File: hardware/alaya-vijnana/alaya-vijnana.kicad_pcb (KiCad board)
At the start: 2 copper layers, 2 parts, among them U2 nRF52840, X1 IQD_85SMX

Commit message: schematics done outside of cluster to main connectors, PCB laid out
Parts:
- added C1: 12pF, Capacitor_SMD:C_0603_1608Metric_Pad1.08x0.95mm_HandSolder, F.Cu at (532.9, 137.2)
- added C10: 100pF, Capacitor_SMD:C_0603_1608Metric_Pad1.08x0.95mm_HandSolder, F.Cu at (537.3, 137.2)
- added C11: 100pF, Capacitor_SMD:C_0603_1608Metric_Pad1.08x0.95mm_HandSolder, F.Cu at (537.3, 139.7)
- added C12: 820pF, Capacitor_SMD:C_0603_1608Metric_Pad1.08x0.95mm_HandSolder, F.Cu at (537.3, 142.2)
- added C13: 4.7uF, Capacitor_SMD:C_0603_1608Metric_Pad1.08x0.95mm_HandSolder, F.Cu at (537.3, 144.7)
- added C14: 1uF, Capacitor_SMD:C_0603_1608Metric_Pad1.08x0.95mm_HandSolder, F.Cu at (537.3, 147.3)
- added C15: 47nF, Capacitor_SMD:C_0603_1608Metric_Pad1.08x0.95mm_HandSolder, F.Cu at (537.3, 149.8)
- added C16: 4.7uF, Capacitor_SMD:C_0603_1608Metric_Pad1.08x0.95mm_HandSolder, F.Cu at (537.3, 152.3)
- added C17: 4.7uF, Capacitor_SMD:C_0603_1608Metric_Pad1.08x0.95mm_HandSolder, F.Cu at (537.3, 154.8)
- added C18: 1uf, Capacitor_SMD:C_0603_1608Metric_Pad1.08x0.95mm_HandSolder, F.Cu at (537.3, 157.3)
- added C19: 100nF, Capacitor_SMD:C_0603_1608Metric_Pad1.08x0.95mm_HandSolder, F.Cu at (541.6, 137.2)
- added C2: 12pF, Capacitor_SMD:C_0603_1608Metric_Pad1.08x0.95mm_HandSolder, F.Cu at (532.9, 139.7)
- added C20: 100nF, Capacitor_SMD:C_0603_1608Metric_Pad1.08x0.95mm_HandSolder, F.Cu at (541.6, 139.7)
- added C21: 100nF, Capacitor_SMD:C_0603_1608Metric_Pad1.08x0.95mm_HandSolder, F.Cu at (541.6, 142.2)
- added C22: 4.7uF, Capacitor_SMD:C_0603_1608Metric_Pad1.08x0.95mm_HandSolder, F.Cu at (541.6, 144.7)
- added C23: 12pF, Capacitor_SMD:C_0603_1608Metric_Pad1.08x0.95mm_HandSolder, F.Cu at (541.6, 147.3)
- added C24: 12pF, Capacitor_SMD:C_0603_1608Metric_Pad1.08x0.95mm_HandSolder, F.Cu at (541.6, 149.8)
- added C25: 4.7uF, Capacitor_SMD:C_0603_1608Metric_Pad1.08x0.95mm_HandSolder, F.Cu at (541.6, 152.3)
- added C26: 1uf, Capacitor_SMD:C_0603_1608Metric_Pad1.08x0.95mm_HandSolder, F.Cu at (532.9, 64.8)
- added C27: 100nF, Capacitor_SMD:C_0603_1608Metric_Pad1.08x0.95mm_HandSolder, F.Cu at (532.9, 67.3)
- added C28: 100nF, Capacitor_SMD:C_0603_1608Metric_Pad1.08x0.95mm_HandSolder, F.Cu at (532.9, 69.8)
- added C29: 100nF, Capacitor_SMD:C_0603_1608Metric_Pad1.08x0.95mm_HandSolder, F.Cu at (532.9, 72.3)
- added C3: 1uF, Capacitor_SMD:C_0603_1608Metric_Pad1.08x0.95mm_HandSolder, F.Cu at (532.9, 142.2)
- added C30: 4.7uF, Capacitor_SMD:C_0603_1608Metric_Pad1.08x0.95mm_HandSolder, F.Cu at (532.9, 74.9)
- added C31: 12pF, Capacitor_SMD:C_0603_1608Metric_Pad1.08x0.95mm_HandSolder, F.Cu at (532.9, 77.4)
- added C32: 12pF, Capacitor_SMD:C_0603_1608Metric_Pad1.08x0.95mm_HandSolder, F.Cu at (532.9, 79.9)
- added C33: 100pF, Capacitor_SMD:C_0603_1608Metric_Pad1.08x0.95mm_HandSolder, F.Cu at (532.9, 82.4)
- added C34: 100pF, Capacitor_SMD:C_0603_1608Metric_Pad1.08x0.95mm_HandSolder, F.Cu at (532.9, 84.9)
- added C35: 820pF, Capacitor_SMD:C_0603_1608Metric_Pad1.08x0.95mm_HandSolder, F.Cu at (537.3, 64.8)
- added C36: 4.7uF, Capacitor_SMD:C_0603_1608Metric_Pad1.08x0.95mm_HandSolder, F.Cu at (537.3, 67.3)
- added C37: 4.7uF, Capacitor_SMD:C_0603_1608Metric_Pad1.08x0.95mm_HandSolder, F.Cu at (537.3, 69.8)
- added C38: 4.7uF, Capacitor_SMD:C_0603_1608Metric_Pad1.08x0.95mm_HandSolder, F.Cu at (537.3, 72.3)
- added C39: 1uF, Capacitor_SMD:C_0603_1608Metric_Pad1.08x0.95mm_HandSolder, F.Cu at (537.3, 74.9)
- added C4: 4.7uF, Capacitor_SMD:C_0603_1608Metric_Pad1.08x0.95mm_HandSolder, F.Cu at (532.9, 144.7)
- added C40: 47nF, Capacitor_SMD:C_0603_1608Metric_Pad1.08x0.95mm_HandSolder, F.Cu at (537.3, 77.4)
- added C41: 12pF, Capacitor_SMD:C_0603_1608Metric_Pad1.08x0.95mm_HandSolder, F.Cu at (537.3, 79.9)
- added C42: 12pF, Capacitor_SMD:C_0603_1608Metric_Pad1.08x0.95mm_HandSolder, F.Cu at (537.3, 82.4)
- added C43: 10uF, Capacitor_SMD:C_0603_1608Metric_Pad1.08x0.95mm_HandSolder, F.Cu at (537.3, 84.9)
- added C44: 1uF, Capacitor_SMD:C_0603_1608Metric_Pad1.08x0.95mm_HandSolder, F.Cu at (541.6, 64.8)
- added C45: 4.7uF, Capacitor_SMD:C_0603_1608Metric_Pad1.08x0.95mm_HandSolder, F.Cu at (541.6, 67.3)
- added C46: 4.7uF, Capacitor_SMD:C_0603_1608Metric_Pad1.08x0.95mm_HandSolder, F.Cu at (541.6, 69.8)
- added C47: 4.7uF, Capacitor_SMD:C_0603_1608Metric_Pad1.08x0.95mm_HandSolder, F.Cu at (541.6, 72.3)
- added C48: 0.8pF, Capacitor_SMD:C_0603_1608Metric_Pad1.08x0.95mm_HandSolder, F.Cu at (541.6, 74.9)
- added C49: 0.5pF, Capacitor_SMD:C_0603_1608Metric_Pad1.08x0.95mm_HandSolder, F.Cu at (541.6, 77.4)
- added C5: 4.7uF, Capacitor_SMD:C_0603_1608Metric_Pad1.08x0.95mm_HandSolder, F.Cu at (532.9, 147.3)
- added C50: N.C., Capacitor_SMD:C_0603_1608Metric_Pad1.08x0.95mm_HandSolder, F.Cu at (541.6, 79.9)
- added C6: 0.8pF, Capacitor_SMD:C_0603_1608Metric_Pad1.08x0.95mm_HandSolder, F.Cu at (532.9, 149.8)
- added C7: 0.5pF, Capacitor_SMD:C_0603_1608Metric_Pad1.08x0.95mm_HandSolder, F.Cu at (532.9, 152.3)
- added C8: N.C., Capacitor_SMD:C_0603_1608Metric_Pad1.08x0.95mm_HandSolder, F.Cu at (532.9, 154.8)
- added C9: 10uF, Capacitor_SMD:C_0603_1608Metric_Pad1.08x0.95mm_HandSolder, F.Cu at (532.9, 157.3)
- added D1: D, Diode_SMD:D_0603_1608Metric_Pad1.05x0.95mm_HandSolder, B.Cu at (236.0, 16.9)
- added D10: D, Diode_SMD:D_0603_1608Metric_Pad1.05x0.95mm_HandSolder, B.Cu at (199.5, 14.0)
- added D11: D, Diode_SMD:D_0603_1608Metric_Pad1.05x0.95mm_HandSolder, B.Cu at (242.8, 22.6)
- added D12: D, Diode_SMD:D_0603_1608Metric_Pad1.05x0.95mm_HandSolder, B.Cu at (183.8, 23.6)
- added D13: D, Diode_SMD:D_0603_1608Metric_Pad1.05x0.95mm_HandSolder, B.Cu at (248.2, 16.4)
- added D14: D, Diode_SMD:D_0603_1608Metric_Pad1.05x0.95mm_HandSolder, B.Cu at (157.5, 6.88)
- added D15: D, Diode_SMD:D_0603_1608Metric_Pad1.05x0.95mm_HandSolder, B.Cu at (247.8, 23.6)
- added D16: D, Diode_SMD:D_0603_1608Metric_Pad1.05x0.95mm_HandSolder, B.Cu at (176.2, 15.1)
- added D17: D, Diode_SMD:D_0603_1608Metric_Pad1.05x0.95mm_HandSolder, B.Cu at (158.0, 20.9)
- added D18: D, Diode_SMD:D_0603_1608Metric_Pad1.05x0.95mm_HandSolder, B.Cu at (256.2, 22.9)
- added D19: D, Diode_SMD:D_0603_1608Metric_Pad1.05x0.95mm_HandSolder, B.Cu at (243.0, 32.9)
- added D2: D, Diode_SMD:D_0603_1608Metric_Pad1.05x0.95mm_HandSolder, B.Cu at (156.0, 13.6)
- added D20: D, Diode_SMD:D_0603_1608Metric_Pad1.05x0.95mm_HandSolder, B.Cu at (168.2, 20.4)
- added D21: D, Diode_SMD:D_0603_1608Metric_Pad1.05x0.95mm_HandSolder, B.Cu at (259.8, 31.4)
- added D22: D, Diode_SMD:D_0603_1608Metric_Pad1.05x0.95mm_HandSolder, B.Cu at (257.0, 15.4)
- added D23: D, Diode_SMD:D_0603_1608Metric_Pad1.05x0.95mm_HandSolder, B.Cu at (158.8, 27.1)
- added D24: D, Diode_SMD:D_0603_1608Metric_Pad1.05x0.95mm_HandSolder, B.Cu at (252.2, 28.6)
- added D25: D, Diode_SMD:D_0603_1608Metric_Pad1.05x0.95mm_HandSolder, B.Cu at (193.2, 12.4)
- added D26: D, Diode_SMD:D_0603_1608Metric_Pad1.05x0.95mm_HandSolder, B.Cu at (164.5, 25.6)
- added D27: D, Diode_SMD:D_0603_1608Metric_Pad1.05x0.95mm_HandSolder, B.Cu at (235.5, 24.1)
- added D28: D, Diode_SMD:D_0603_1608Metric_Pad1.05x0.95mm_HandSolder, B.Cu at (262.2, 24.1)
- added D29: D, Diode_SMD:D_0603_1608Metric_Pad1.05x0.95mm_HandSolder, B.Cu at (164.1, 36.5)
- added D3: D, Diode_SMD:D_0603_1608Metric_Pad1.05x0.95mm_HandSolder, B.Cu at (240.5, 11.9)
- added D30: D, Diode_SMD:D_0603_1608Metric_Pad1.05x0.95mm_HandSolder, B.Cu at (186.7, 42.6)
- added D31: D, Diode_SMD:D_0603_1608Metric_Pad1.05x0.95mm_HandSolder, B.Cu at (174.9, 30.0)
- added D32: D, Diode_SMD:D_0603_1608Metric_Pad1.05x0.95mm_HandSolder, B.Cu at (178.7, 31.7)
- added D33: D, Diode_SMD:D_0603_1608Metric_Pad1.05x0.95mm_HandSolder, B.Cu at (191.2, 42.7)
- added D34: D, Diode_SMD:D_0603_1608Metric_Pad1.05x0.95mm_HandSolder, B.Cu at (195.2, 44.4)
- added D35: D, Diode_SMD:D_0603_1608Metric_Pad1.05x0.95mm_HandSolder, B.Cu at (206.7, 37.7)
- added D36: D, Diode_SMD:D_0603_1608Metric_Pad1.05x0.95mm_HandSolder, B.Cu at (212.4, 38.7)
- added D37: D, Diode_SMD:D_0603_1608Metric_Pad1.05x0.95mm_HandSolder, B.Cu at (230.2, 42.4)
- added D38: D, Diode_SMD:D_0603_1608Metric_Pad1.05x0.95mm_HandSolder, B.Cu at (223.1, 40.3)
- added D39: D, Diode_SMD:D_0603_1608Metric_Pad1.05x0.95mm_HandSolder, B.Cu at (218.2, 39.2)
- added D4: D, Diode_SMD:D_0603_1608Metric_Pad1.05x0.95mm_HandSolder, B.Cu at (163.5, 6.88)
- added D40: D, Diode_SMD:D_0603_1608Metric_Pad1.05x0.95mm_HandSolder, B.Cu at (230.1, 32.5)
- added D41: D, Diode_SMD:D_0603_1608Metric_Pad1.05x0.95mm_HandSolder, B.Cu at (185.5, 13.4)
- added D42: D, Diode_SMD:D_0603_1608Metric_Pad1.05x0.95mm_HandSolder, B.Cu at (169.5, 13.9)
- added D5: D, Diode_SMD:D_0603_1608Metric_Pad1.05x0.95mm_HandSolder, B.Cu at (232.5, 9.62)
- added D6: D, Diode_SMD:D_0603_1608Metric_Pad1.05x0.95mm_HandSolder, B.Cu at (162.0, 13.4)
- added D7: D, Diode_SMD:D_0603_1608Metric_Pad1.05x0.95mm_HandSolder, B.Cu at (163.8, 20.1)
- added D8: D, Diode_SMD:D_0603_1608Metric_Pad1.05x0.95mm_HandSolder, B.Cu at (226.0, 14.0)
- added D9: D, Diode_SMD:D_0603_1608Metric_Pad1.05x0.95mm_HandSolder, B.Cu at (248.8, 8.88)
- added J1: Bat, Connector_JST:JST_PH_S2B-PH-K_1x02_P2.00mm_Horizontal, F.Cu at (562.7, 156.2)
- added J2: USB_C_Receptacle_USB2.0_16P, Connector_USB:USB_C_Receptacle_GCT_USB4085, F.Cu at (551.0, 155.4)
- added J3: Bat, Connector_JST:JST_PH_S2B-PH-K_1x02_P2.00mm_Horizontal, F.Cu at (562.7, 83.8)
- added J4: USB_C_Receptacle_USB2.0_16P, Connector_USB:USB_C_Receptacle_GCT_USB4085, F.Cu at (551.0, 83.0)
- added L1: 4.7nH, Inductor_SMD:L_0402_1005Metric_Pad0.77x0.64mm_HandSolder, F.Cu at (565.4, 144.5)
- added L2: 10uH, Inductor_SMD:L_0603_1608Metric, F.Cu at (565.8, 137.2)
- added L3: 15nH, Inductor_SMD:L_0603_1608Metric, F.Cu at (565.8, 139.7)
- added L4: 10uH, Inductor_SMD:L_0603_1608Metric, F.Cu at (565.8, 142.2)
- added L5: 15nH, Inductor_SMD:L_0603_1608Metric, F.Cu at (565.8, 64.8)
- added L6: 10uH, Inductor_SMD:L_0603_1608Metric, F.Cu at (565.8, 67.3)
- added L7: 10uH, Inductor_SMD:L_0603_1608Metric, F.Cu at (565.8, 69.8)
- added L8: 4.7nH, Inductor_SMD:L_0402_1005Metric_Pad0.77x0.64mm_HandSolder, F.Cu at (565.4, 72.1)
- added LED1: Charge_LED, PCM_LED_SMD_AKL:LED_1206_3216Metric, F.Cu at (543.7, 160.7)
- added LED2: Charge_LED, PCM_LED_SMD_AKL:LED_1206_3216Metric, F.Cu at (543.7, 88.3)
- added R1: 2k, Resistor_SMD:R_0603_1608Metric_Pad0.98x0.95mm_HandSolder, F.Cu at (541.6, 154.8)
- added R10: 10M, Resistor_SMD:R_0603_1608Metric_Pad0.98x0.95mm_HandSolder, F.Cu at (546.0, 64.8)
- added R11: 10k, Resistor_SMD:R_0603_1608Metric_Pad0.98x0.95mm_HandSolder, F.Cu at (546.0, 67.3)
- added R12: 10k, Resistor_SMD:R_0603_1608Metric_Pad0.98x0.95mm_HandSolder, F.Cu at (546.0, 69.8)
- added R13: 5.1k, Resistor_SMD:R_0603_1608Metric_Pad0.98x0.95mm_HandSolder, F.Cu at (546.0, 72.3)
- added R14: 5.1k, Resistor_SMD:R_0603_1608Metric_Pad0.98x0.95mm_HandSolder, F.Cu at (546.0, 74.9)
- added R2: 10k, Resistor_SMD:R_0603_1608Metric_Pad0.98x0.95mm_HandSolder, F.Cu at (541.6, 157.3)
- added R3: 10k, Resistor_SMD:R_0603_1608Metric_Pad0.98x0.95mm_HandSolder, F.Cu at (546.0, 137.2)
- added R4: 10k, Resistor_SMD:R_0603_1608Metric_Pad0.98x0.95mm_HandSolder, F.Cu at (546.0, 139.7)
- added R5: 10M, Resistor_SMD:R_0603_1608Metric_Pad0.98x0.95mm_HandSolder, F.Cu at (546.0, 142.2)
- added R6: 5.1k, Resistor_SMD:R_0603_1608Metric_Pad0.98x0.95mm_HandSolder, F.Cu at (546.0, 144.7)
- added R7: 5.1k, Resistor_SMD:R_0603_1608Metric_Pad0.98x0.95mm_HandSolder, F.Cu at (546.0, 147.3)
- added R8: 2k, Resistor_SMD:R_0603_1608Metric_Pad0.98x0.95mm_HandSolder, F.Cu at (541.6, 82.4)
- added R9: 10k, Resistor_SMD:R_0603_1608Metric_Pad0.98x0.95mm_HandSolder, F.Cu at (541.6, 84.9)
- added SW1: Power_Switch, Button_Switch_THT:SW_E-Switch_EG1224_SPDT_Angled, B.Cu at (516.4, 156.7)
- added SW10: MX HotSwap, MX_Hotswap:MX-Hotswap-1U, B.Cu at (74.8, 90.9)
- added SW11: MX HotSwap, MX_Hotswap:MX-Hotswap-1U, B.Cu at (93.9, 62.3)
- added SW12: MX HotSwap, MX_Hotswap:MX-Hotswap-1U, B.Cu at (93.9, 81.4)
- added SW13: MX HotSwap, MX_Hotswap:MX-Hotswap-1U, B.Cu at (93.9, 100.4)
- added SW14: MX HotSwap, MX_Hotswap:MX-Hotswap-1U, B.Cu at (112.9, 67.1)
- added SW15: MX HotSwap, MX_Hotswap:MX-Hotswap-1U, B.Cu at (112.9, 86.1)
- added SW16: MX HotSwap, MX_Hotswap:MX-Hotswap-1U, B.Cu at (112.9, 105.2)
- added SW17: MX HotSwap, MX_Hotswap:MX-Hotswap-1U, B.Cu at (151.9, 120.7)
- added SW18: MX HotSwap, MX_Hotswap:MX-Hotswap-2U, B.Cu at (137.6, 145.5)
- added SW19: MX HotSwap, MX_Hotswap:MX-Hotswap-2U, B.Cu at (121.2, 136.0)
- added SW2: MX HotSwap, MX_Hotswap:MX-Hotswap-1U, B.Cu at (36.7, 67.1)
- added SW20: MX HotSwap, MX_Hotswap:MX-Hotswap-1U, B.Cu at (168.4, 130.3)
- added SW21: MX HotSwap, MX_Hotswap:MX-Hotswap-1U, B.Cu at (158.9, 146.8)
- added SW22: MX HotSwap, MX_Hotswap:MX-Hotswap-1U, B.Cu at (149.4, 163.3)
- added SW23: Power_Switch, Button_Switch_THT:SW_E-Switch_EG1224_SPDT_Angled, B.Cu at (506.4, 76.2)
- added SW24: MX HotSwap, MX_Hotswap:MX-Hotswap-1U, B.Cu at (371.5, 71.4)
- added SW25: MX HotSwap, MX_Hotswap:MX-Hotswap-1U, B.Cu at (371.5, 90.5)
- added SW26: MX HotSwap, MX_Hotswap:MX-Hotswap-1U, B.Cu at (371.5, 109.5)
- added SW27: MX HotSwap, MX_Hotswap:MX-Hotswap-1U, B.Cu at (352.4, 61.9)
- added SW28: MX HotSwap, MX_Hotswap:MX-Hotswap-1U, B.Cu at (352.4, 81.0)
- added SW29: MX HotSwap, MX_Hotswap:MX-Hotswap-1U, B.Cu at (352.4, 100.0)
- added SW3: MX HotSwap, MX_Hotswap:MX-Hotswap-1U, B.Cu at (36.7, 86.1)
- added SW30: MX HotSwap, MX_Hotswap:MX-Hotswap-1U, B.Cu at (333.4, 57.1)
- added SW31: MX HotSwap, MX_Hotswap:MX-Hotswap-1U, B.Cu at (333.4, 76.2)
- added SW32: MX HotSwap, MX_Hotswap:MX-Hotswap-1U, B.Cu at (333.4, 95.2)
- added SW33: MX HotSwap, MX_Hotswap:MX-Hotswap-1U, B.Cu at (314.3, 66.7)
- added SW34: MX HotSwap, MX_Hotswap:MX-Hotswap-1U, B.Cu at (314.3, 85.7)
- added SW35: MX HotSwap, MX_Hotswap:MX-Hotswap-1U, B.Cu at (314.3, 104.8)
- added SW36: MX HotSwap, MX_Hotswap:MX-Hotswap-1U, B.Cu at (295.3, 71.4)
- added SW37: MX HotSwap, MX_Hotswap:MX-Hotswap-1U, B.Cu at (295.3, 90.5)
- added SW38: MX HotSwap, MX_Hotswap:MX-Hotswap-1U, B.Cu at (295.3, 109.5)
- added SW39: MX HotSwap, MX_Hotswap:MX-Hotswap-1U, B.Cu at (249.3, 151.1)
- added SW4: MX HotSwap, MX_Hotswap:MX-Hotswap-1U, B.Cu at (36.7, 105.2)
- added SW40: MX HotSwap, MX_Hotswap:MX-Hotswap-2U, B.Cu at (270.5, 149.8)
- added SW41: MX HotSwap, MX_Hotswap:MX-Hotswap-2U, B.Cu at (287.0, 140.3)
- added SW42: MX HotSwap, MX_Hotswap:MX-Hotswap-1U, B.Cu at (258.8, 167.6)
- added SW43: MX HotSwap, MX_Hotswap:MX-Hotswap-1U, B.Cu at (256.2, 125.1)
- added SW44: MX HotSwap, MX_Hotswap:MX-Hotswap-1U, B.Cu at (239.7, 134.6)
- added SW5: MX HotSwap, MX_Hotswap:MX-Hotswap-1U, B.Cu at (55.8, 57.5)
- added SW6: MX HotSwap, MX_Hotswap:MX-Hotswap-1U, B.Cu at (55.8, 76.6)
- added SW7: MX HotSwap, MX_Hotswap:MX-Hotswap-1U, B.Cu at (55.8, 95.6)
- added SW8: MX HotSwap, MX_Hotswap:MX-Hotswap-1U, B.Cu at (74.8, 52.8)
- added SW9: MX HotSwap, MX_Hotswap:MX-Hotswap-1U, B.Cu at (74.8, 71.8)
- added TP1: Charge Boost, Resistor_SMD:R_2816_7142Metric_Pad3.20x4.45mm_HandSolder, F.Cu at (553.1, 168.1)
- added TP2: Charge Boost, Resistor_SMD:R_2816_7142Metric_Pad3.20x4.45mm_HandSolder, F.Cu at (553.1, 95.7)
- added U1: nRF52840, Package_DFN_QFN:Nordic_AQFN-73-1EP_7x7mm_P0.5mm, F.Cu at (535.8, 163.6)
- added U3: XC6220B331MR, Package_TO_SOT_SMD:SOT-23-5, F.Cu at (543.4, 170.6)
- added U4: nRF52840, Package_DFN_QFN:Nordic_AQFN-73-1EP_7x7mm_P0.5mm, F.Cu at (535.8, 91.2)
- added U5: XC6220B331MR, Package_TO_SOT_SMD:SOT-23-5, F.Cu at (543.4, 98.2)
- added U6: BQ24075RGT, Package_DFN_QFN:VQFN-16-1EP_3x3mm_P0.5mm_EP1.6x1.6mm, F.Cu at (543.8, 93.1)
- added X2: 32.768kHz, Crystal:Crystal_SMD_2012-2Pin_2.0x1.2mm, F.Cu at (561.8, 98.5)
- added Y1: 32Mhz, Crystal:Crystal_SMD_3225-4Pin_3.2x2.5mm_HandSoldering, F.Cu at (563.1, 166.4)
- added Y2: 32Mhz, Crystal:Crystal_SMD_3225-4Pin_3.2x2.5mm_HandSoldering, F.Cu at (563.1, 94.0)
- U2: value nRF52840 -> BQ24075RGT; footprint Package_DFN_QFN:Nordic_AQFN-73-1EP_7x7mm_P0.5mm -> Package_DFN_QFN:VQFN-16-1EP_3x3mm_P0.5mm_EP1.6x1.6mm
- X1: value IQD_85SMX -> 32.768kHz; footprint PCM_Crystal_AKL:Crystal_SMD_8.7x3.8mm_P5.50mm -> Crystal:Crystal_SMD_2012-2Pin_2.0x1.2mm
- moved X1 438.8 mm to (561.8, 170.9)
- moved U2 419.5 mm to (543.8, 165.5)
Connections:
- X1 pad 2: unconnected-(X1-NC-Pad2) -> Net-(U1-XL1/P0.00)

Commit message: finished key wiring w/ connectors
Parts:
- added J5: MAIN_CONN, Connector_IDC:IDC-Header_2x03_P2.54mm_Horizontal, B.Cu at (110.5, 116.3)
- added J6: MAIN_CONN, Connector_IDC:IDC-Header_2x03_P2.54mm_Horizontal, F.Cu at (474.3, 124.2)
- added J7: CLUSTER_CONN, Connector_IDC:IDC-Header_2x03_P2.54mm_Horizontal, B.Cu at (295.6, 164.3)
- added J8: CLUSTER_CONN, Connector_IDC:IDC-Header_2x03_P2.54mm_Horizontal, B.Cu at (115.0, 154.2)
- J1, J2: moved to B.Cu
- moved TP1 572.2 mm to (-13.6, 89.0)
- moved R3 517.8 mm to (70.3, -67.5)
- moved R4 517.8 mm to (70.3, -65.0)
- moved R5 517.8 mm to (70.3, -62.5)
- moved C1 517.8 mm to (57.3, -67.5)
- moved C10 517.8 mm to (61.6, -67.5)
- moved C11 517.8 mm to (61.6, -65.0)
- moved C12 517.8 mm to (61.6, -62.5)
- moved C13 517.8 mm to (61.6, -60.0)
- moved C14 517.8 mm to (61.6, -57.5)
- moved C15 517.8 mm to (61.6, -55.0)
- moved C16 517.8 mm to (61.6, -52.5)
- moved C17 517.8 mm to (61.6, -50.0)
- moved C18 517.8 mm to (61.6, -47.4)
- moved C19 517.8 mm to (66.0, -67.5)
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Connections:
- net COL5 renamed C_COL5
- net COL6 renamed C_COL6
- net L_COL5 renamed LC_COL5
- net L_COL6 renamed LC_COL6
- C1 pad 2: L_VSS_PA -> L_BAT-
- C10 pad 1: L_VSS_PA -> L_BAT-
- C11 pad 1: L_VSS_PA -> L_BAT-
- C12 pad 1: L_VSS_PA -> L_BAT-
- C13 pad 1: L_VSS_PA -> L_BAT-
- C14 pad 2: L_VSS_PA -> L_BAT-
- C15 pad 2: L_VSS_PA -> L_BAT-
- C16 pad 1: L_VSS_PA -> L_BAT-
- C17 pad 2: L_VSS_PA -> L_BAT-
- C18 pad 2: L_VSS_PA -> L_BAT-
- C19 pad 2: L_VSS_PA -> L_BAT-
- C2 pad 2: L_VSS_PA -> L_BAT-
- C20 pad 2: L_VSS_PA -> L_BAT-
- C21 pad 2: L_VSS_PA -> L_BAT-
- C22 pad 2: L_VSS_PA -> L_BAT-
- C23 pad 1: L_VSS_PA -> L_BAT-
- C24 pad 1: L_VSS_PA -> L_BAT-
- C25 pad 2: L_VSS_PA -> L_BAT-
- C26 pad 2: L_VSS_PA -> L_BAT-
- C27 pad 2: L_VSS_PA -> L_BAT-
- C28 pad 2: L_VSS_PA -> L_BAT-
- C29 pad 2: L_VSS_PA -> L_BAT-
- C3 pad 1: L_VSS_PA -> L_BAT-
- C30 pad 2: L_VSS_PA -> L_BAT-
- C31 pad 2: L_VSS_PA -> L_BAT-
- C32 pad 2: L_VSS_PA -> L_BAT-
- C33 pad 1: L_VSS_PA -> L_BAT-
- C34 pad 1: L_VSS_PA -> L_BAT-
- C35 pad 1: L_VSS_PA -> L_BAT-
- C36 pad 1: L_VSS_PA -> L_BAT-
- C37 pad 1: L_VSS_PA -> L_BAT-
- C38 pad 2: L_VSS_PA -> L_BAT-
- C39 pad 2: L_VSS_PA -> L_BAT-
- C4 pad 2: L_VSS_PA -> L_BAT-
- C40 pad 2: L_VSS_PA -> L_BAT-
- C41 pad 1: L_VSS_PA -> L_BAT-
- C42 pad 1: L_VSS_PA -> L_BAT-
- C43 pad 2: L_VSS_PA -> L_BAT-
- C44 pad 1: L_VSS_PA -> L_BAT-
- C45 pad 2: L_VSS_PA -> L_BAT-
- C47 pad 2: L_VSS_PA -> L_BAT-
- C48 pad 2: L_VSS_PA -> L_BAT-
- C49 pad 2: L_VSS_PA -> L_BAT-
- C50 pad 2: L_VSS_PA -> L_BAT-
- C6 pad 2: L_VSS_PA -> L_BAT-
- C7 pad 2: L_VSS_PA -> L_BAT-
- C8 pad 2: L_VSS_PA -> L_BAT-
- C9 pad 2: L_VSS_PA -> L_BAT-
- D16 pad 1: L_ROW0 -> LC_ROW0
- D17 pad 1: L_ROW1 -> LC_ROW1
- D18 pad 1: L_ROW2 -> LC_ROW2
- D19 pad 1: L_ROW0 -> LC_ROW0
- D20 pad 1: L_ROW1 -> LC_ROW1
- D21 pad 1: L_ROW2 -> LC_ROW2
- D37 pad 1: ROW0 -> C_ROW0
- D38 pad 1: ROW1 -> C_ROW1
- D39 pad 1: ROW2 -> C_ROW2
- D40 pad 1: ROW0 -> C_ROW0
- D41 pad 1: ROW1 -> C_ROW1
- D42 pad 1: ROW2 -> C_ROW2
- J2 pad A1: L_VSS_PA -> L_BAT-
- J2 pad A12: L_VSS_PA -> L_BAT-
- J2 pad B1: L_VSS_PA -> L_BAT-
- J2 pad B12: L_VSS_PA -> L_BAT-
- J4 pad A1: L_VSS_PA -> L_BAT-
- J4 pad A12: L_VSS_PA -> L_BAT-
- J4 pad B1: L_VSS_PA -> L_BAT-
- J4 pad B12: L_VSS_PA -> L_BAT-
- R1 pad 1: L_VSS_PA -> L_BAT-
- R11 pad 2: L_VSS_PA -> L_BAT-
- R13 pad 2: L_VSS_PA -> L_BAT-
- R14 pad 2: L_VSS_PA -> L_BAT-
- R2 pad 2: L_VSS_PA -> L_BAT-
- R3 pad 2: L_VSS_PA -> L_BAT-
- R6 pad 2: L_VSS_PA -> L_BAT-
- R7 pad 2: L_VSS_PA -> L_BAT-
- R8 pad 1: L_VSS_PA -> L_BAT-
- R9 pad 2: L_VSS_PA -> L_BAT-
- U1 pad B7: L_VSS_PA -> L_BAT-
- U1 pad EP: L_VSS_PA -> L_BAT-
- U1 pad F23: L_VSS_PA -> L_BAT-
- U2 pad 15: L_VSS_PA -> L_BAT-
- U2 pad 17: L_VSS_PA -> L_BAT-
- U2 pad 4: L_VSS_PA -> L_BAT-
- U2 pad 5: L_VSS_PA -> L_BAT-
- U2 pad 8: L_VSS_PA -> L_BAT-
- U3 pad 2: L_VSS_PA -> L_BAT-
- U4 pad B7: L_VSS_PA -> L_BAT-
- U4 pad EP: L_VSS_PA -> L_BAT-
- U4 pad F23: L_VSS_PA -> L_BAT-
- U5 pad 2: L_VSS_PA -> L_BAT-
- U6 pad 15: L_VSS_PA -> L_BAT-
- U6 pad 17: L_VSS_PA -> L_BAT-
- U6 pad 4: L_VSS_PA -> L_BAT-
- U6 pad 5: L_VSS_PA -> L_BAT-
- U6 pad 8: L_VSS_PA -> L_BAT-
- Y1 pad 2: L_VSS_PA -> L_BAT-
- Y2 pad 2: L_VSS_PA -> L_BAT-
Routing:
- net C_ROW2: track 0.00 -> 100.1 mm
- net L_ROW2: track 0.00 -> 96.1 mm
- net L_ROW1: track 0.00 -> 95.2 mm
- net L_ROW0: track 0.00 -> 92.1 mm
- net LC_COL6: track 0.00 -> 83.8 mm, vias 0 -> 3
- net C_ROW1: track 0.00 -> 79.3 mm
- net C_COL6: track 0.00 -> 67.7 mm, vias 0 -> 3
- net LC_ROW2: track 0.00 -> 67.6 mm
- net LC_COL5: track 0.00 -> 60.7 mm, vias 0 -> 3
- net LC_ROW1: track 0.00 -> 57.1 mm
- net C_COL5: track 0.00 -> 53.0 mm, vias 0 -> 3
- net C_ROW0: track 0.00 -> 45.4 mm
- net L_COL3: track 0.00 -> 38.1 mm, vias 0 -> 3
- net L_COL2: track 0.00 -> 38.1 mm, vias 0 -> 3
- net L_COL1: track 0.00 -> 38.1 mm, vias 0 -> 3
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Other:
- copper layers 2 -> 4

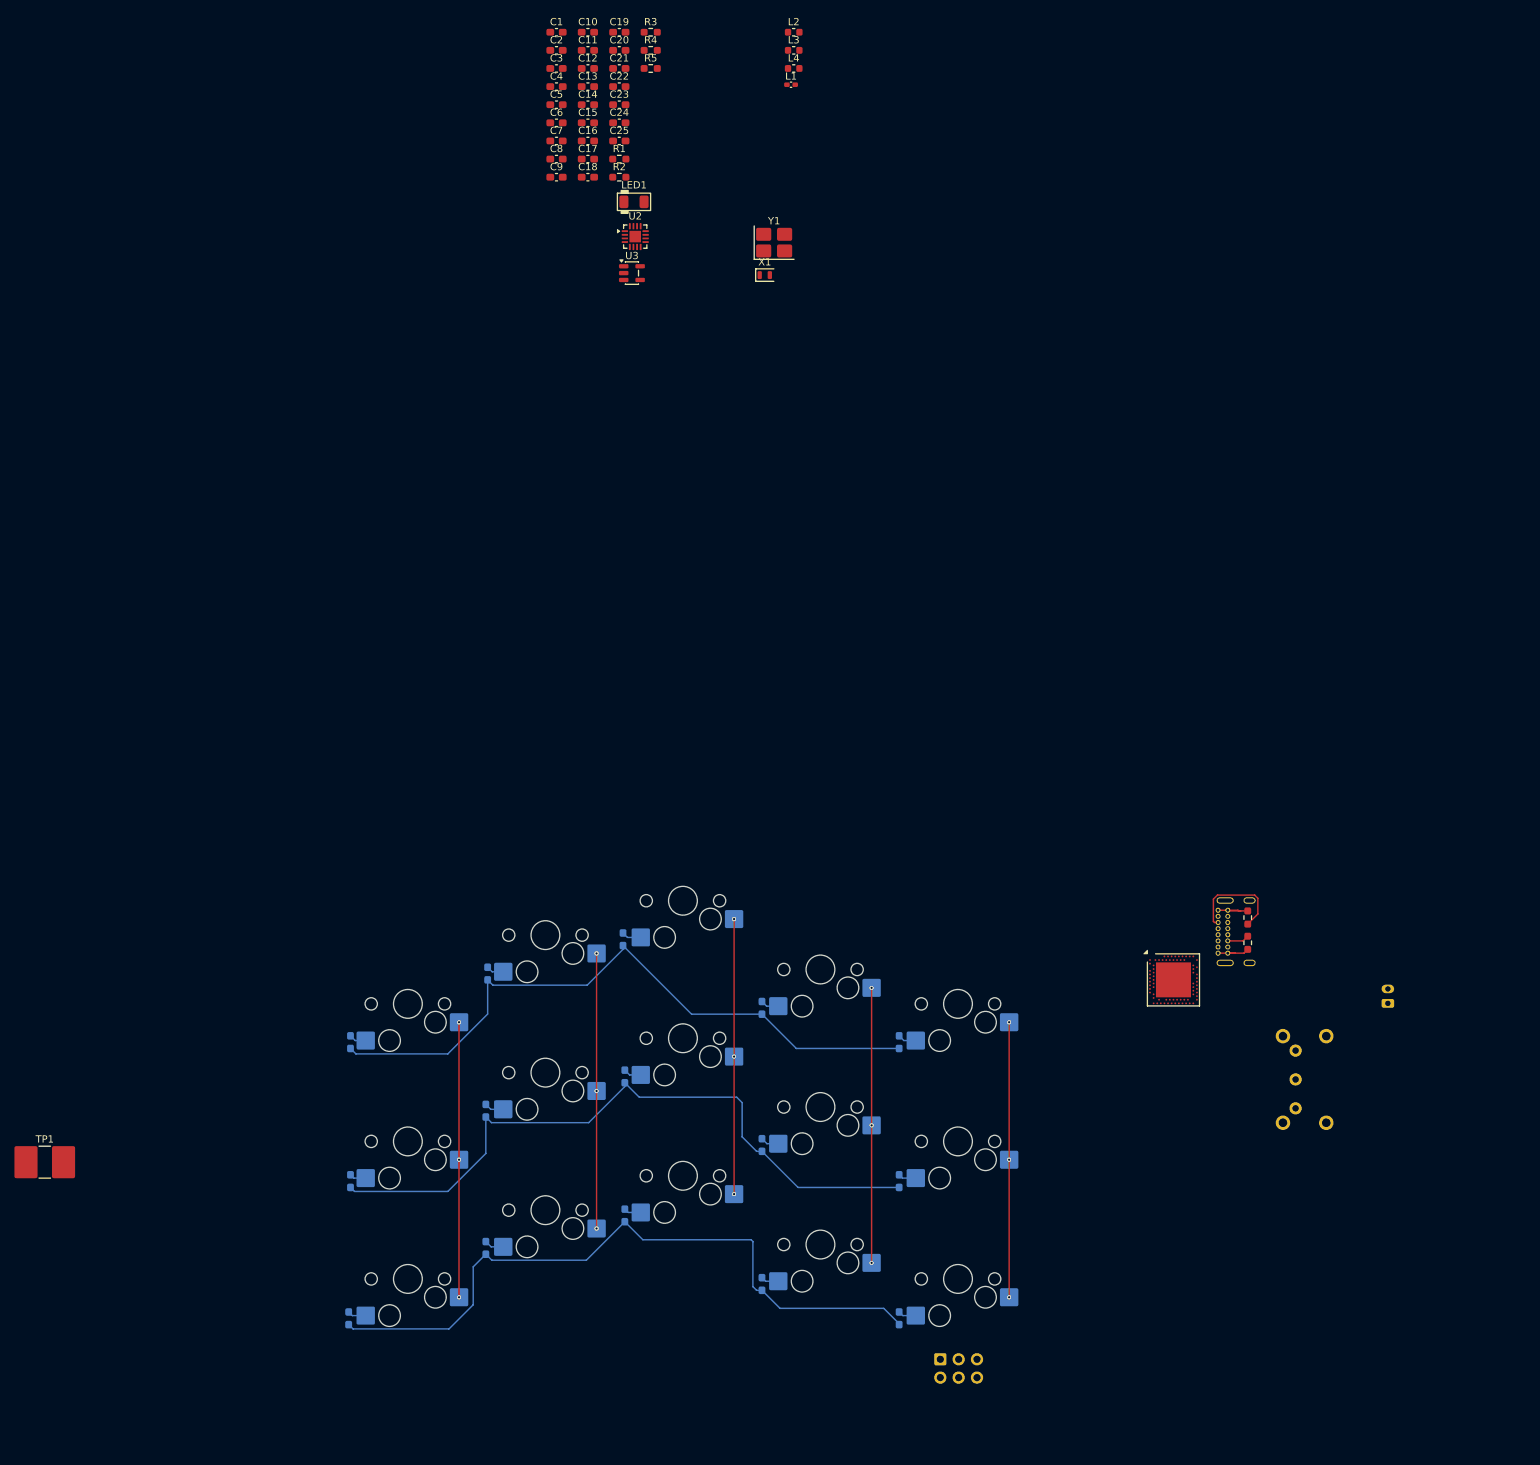
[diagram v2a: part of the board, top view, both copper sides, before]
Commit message: added pcb antenna
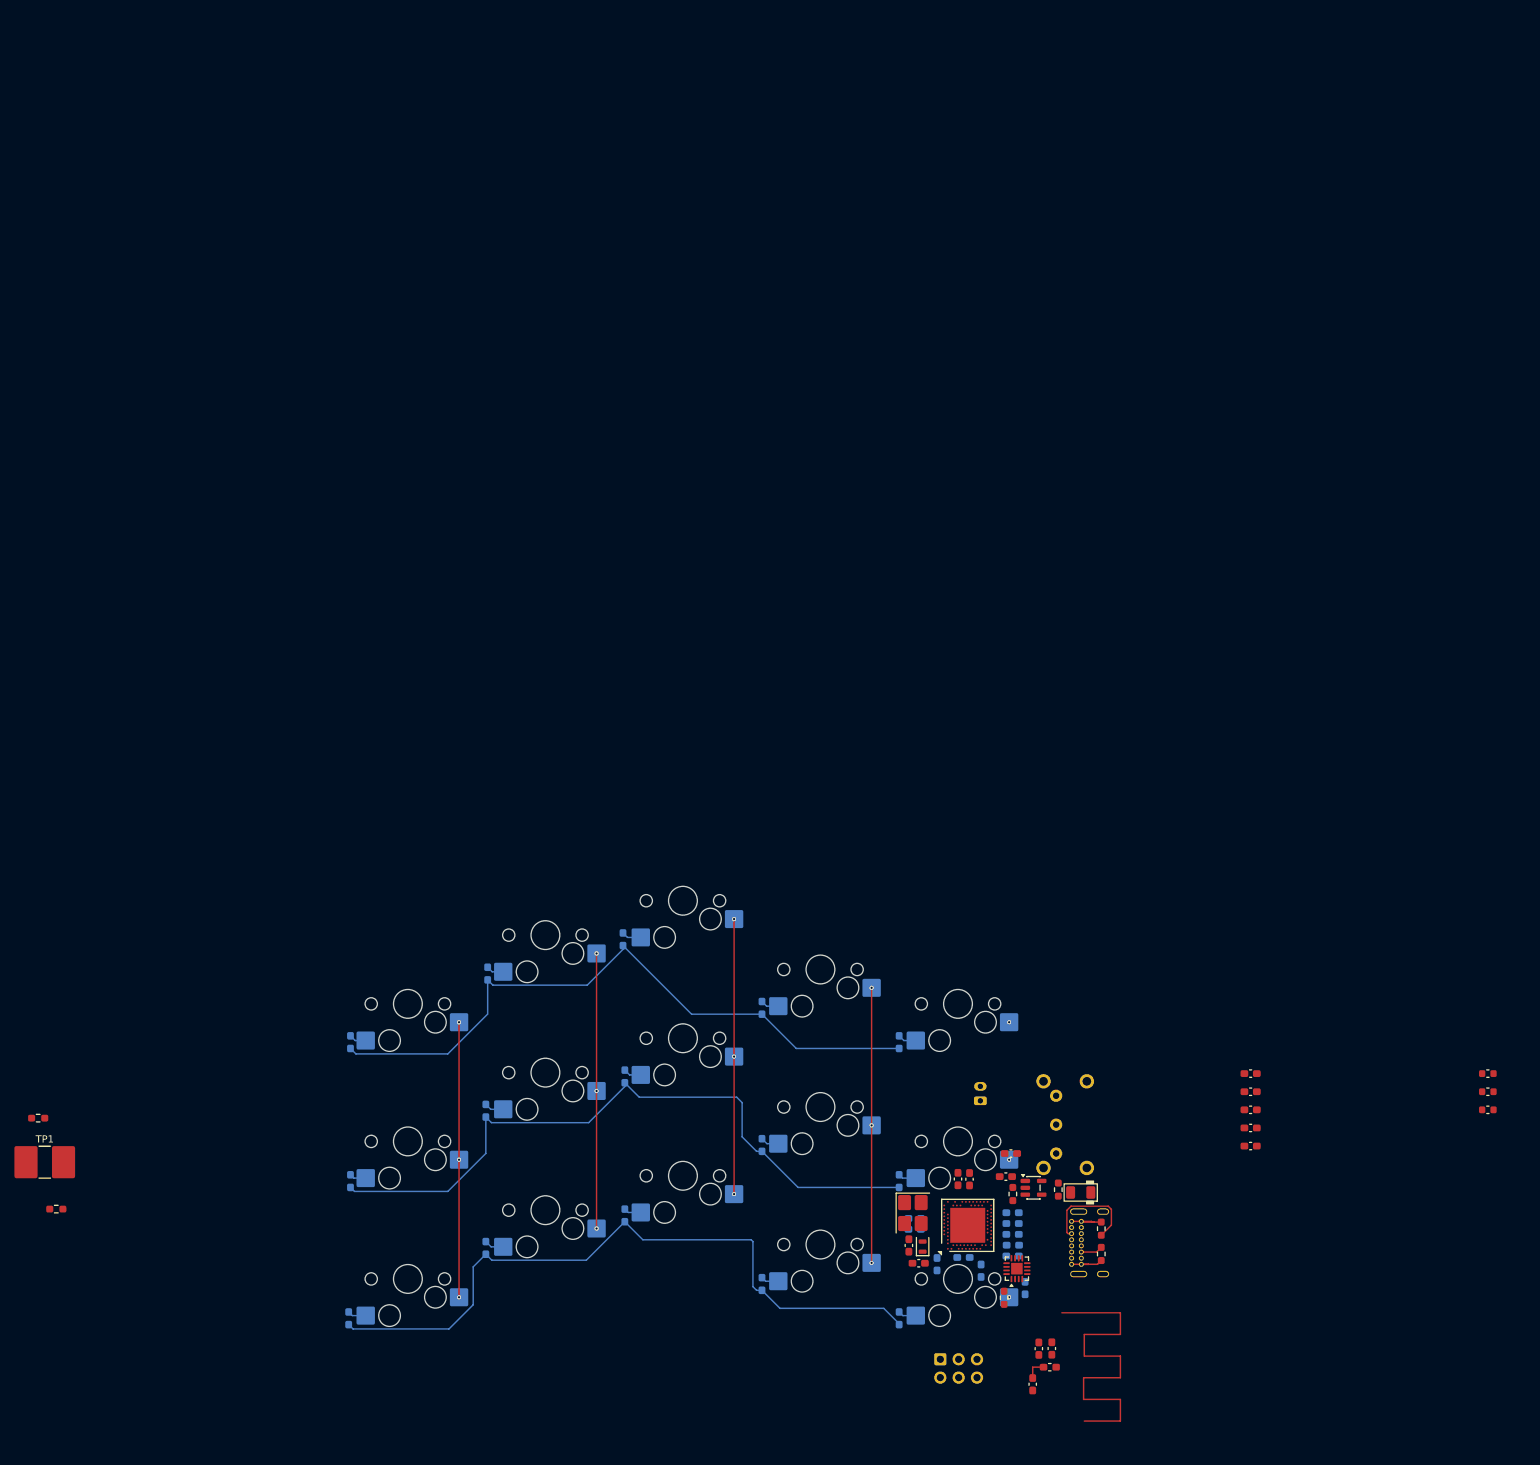
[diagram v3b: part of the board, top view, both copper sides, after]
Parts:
- C10, C13, C14, C15, C16, C17, C18, C19, C20, C21, C22: moved to B.Cu
- L1: footprint Inductor_SMD:L_0402_1005Metric_Pad0.77x0.64mm_HandSolder -> Inductor_SMD:L_0603_1608Metric_Pad1.05x0.95mm_HandSolder
- moved C6 186.8 mm to (123.2, 119.8), turned to -90 degrees
- moved R3 182.0 mm to (119.3, 107.8), turned to -90 degrees
- moved L1 181.2 mm to (125.6, 117.4)
- moved C7 180.1 mm to (124.1, 114.8), turned to -90 degrees
- moved C8 178.5 mm to (125.9, 114.8), turned to -90 degrees
- moved C19 178.1 mm to (120.5, 102.0)
- moved C10 177.4 mm to (110.0, 103.1), turned to 90 degrees
- moved C13 177.1 mm to (122.2, 106.4), turned to 90 degrees
- moved C20 174.3 mm to (120.5, 100.5)
- moved C1 173.4 mm to (153.4, 76.7)
- moved C2 173.4 mm to (153.4, 79.2)
- moved C3 173.4 mm to (153.4, 81.8)
- moved C4 173.4 mm to (153.4, 84.3)
- moved C5 173.4 mm to (153.4, 86.8)
- moved L2 173.4 mm to (186.3, 76.7)
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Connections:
- Y1 pad 4: (no net) -> L_BAT-
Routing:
- net L_RF: track 0.00 -> 48.3 mm
- net L_COL4: track 38.1 -> 0.00 mm
- net L_ANT: track 0.00 -> 3.00 mm
